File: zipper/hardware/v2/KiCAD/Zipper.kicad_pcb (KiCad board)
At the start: 6 copper layers, 107 x 78 mm, 945 parts, among them J1 FX10B-80S/8-SV, J2 FX10B-80S/8-SV, J3 ASP-122952-01_(HSMC), J4 ASP-134604-01, J5 JUMPER2, J6 MINI-USB-UX60A-MB-5ST, J7 PINHEADER2X25, J8 SMA, SW1 SW, SW2 SW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

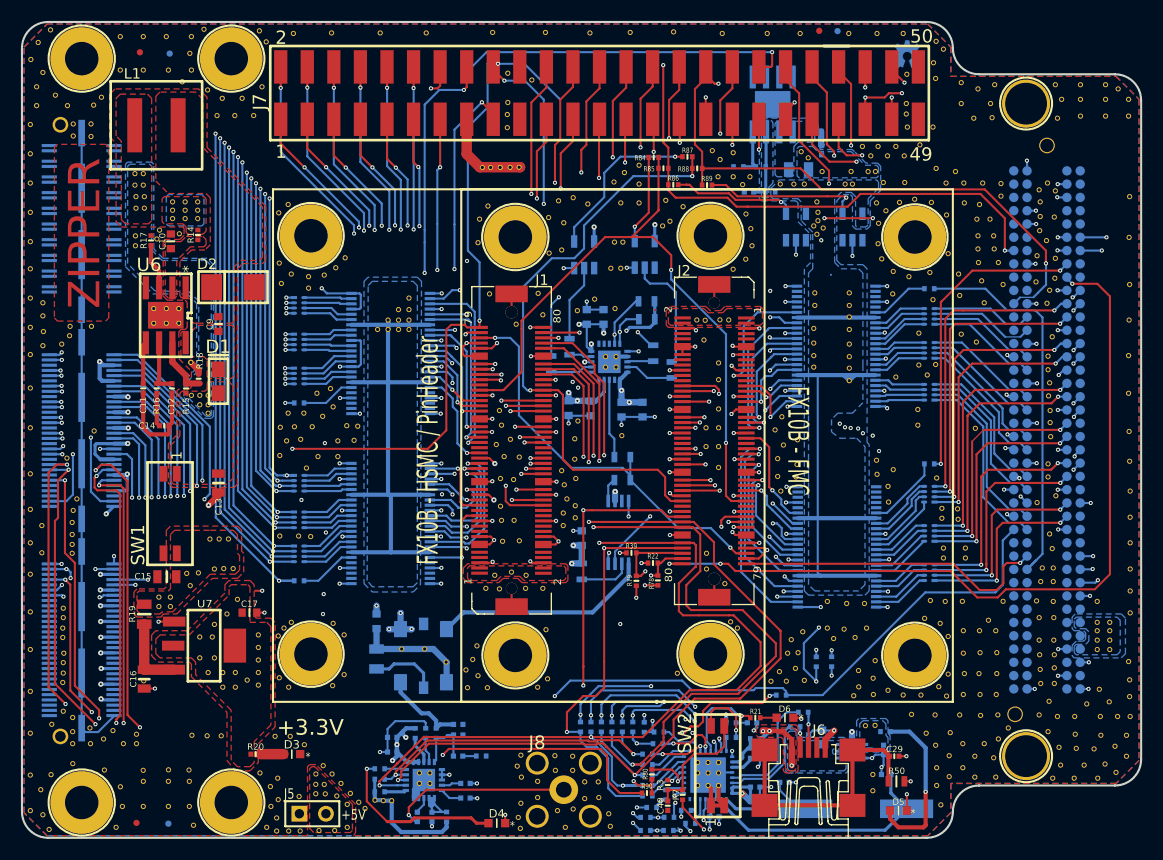
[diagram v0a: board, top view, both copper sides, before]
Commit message: Updated dev kit PDF, and hardware design for placement error
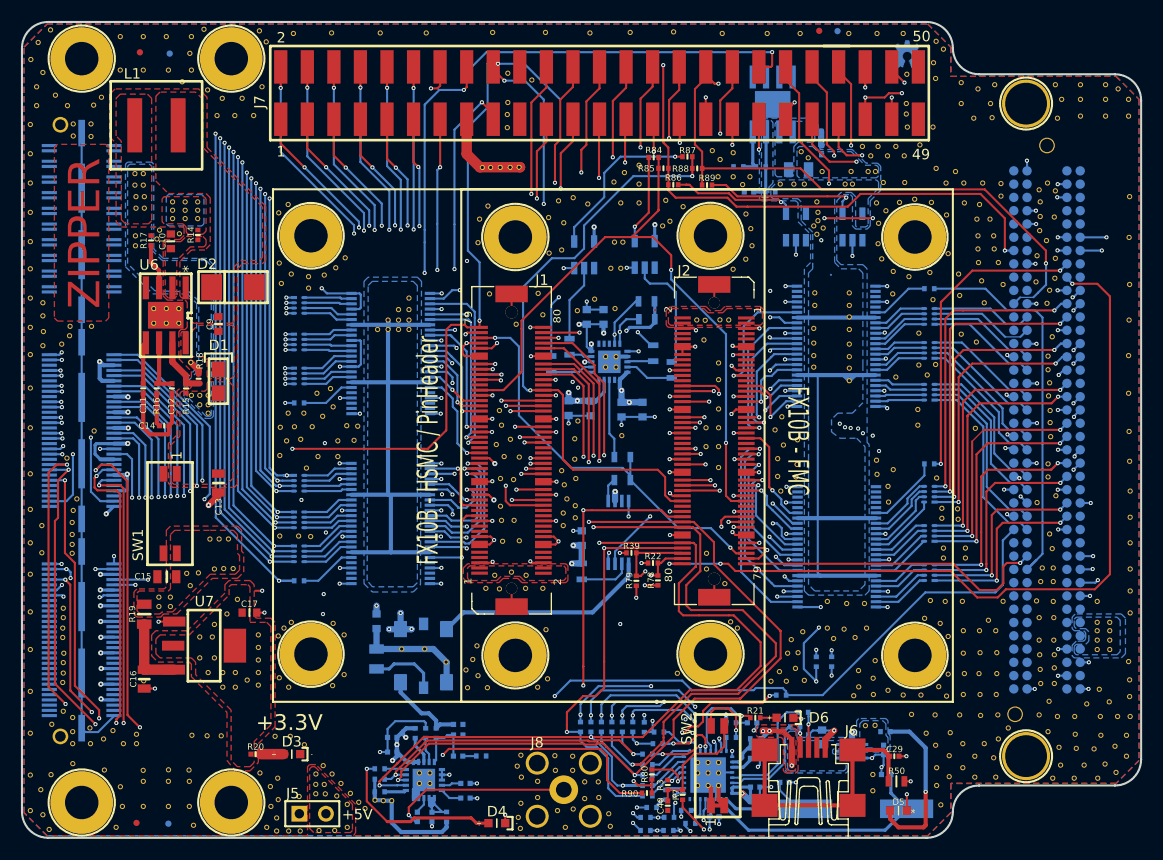
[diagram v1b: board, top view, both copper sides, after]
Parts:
- R84, R86, R87, R89: value 0R_0603 -> 0R_0402
- R85, R88: value 0R_0603_NF -> 0R_0402_NF
- U15: value AT90USB162-16AU -> AT90USB162-16MU
- moved U10 13.7 mm to (167.7, 100.4), turned to 180 degrees
- moved U14 13.7 mm to (117.5, 93.5), turned to 0 degrees
- renumbered U17 to U1, U18 to U12, U1 to X2, U12 to X3
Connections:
- R29 pad 5: N-00000401 -> N-00000399
- R29 pad 6: N-00000407 -> N-00000433
- R29 pad 7: N-00000394 (its old number) -> N-00000402
- R29 pad 8: N-00000397 -> N-00000404
- R30 pad 5: N-00000396 -> N-00000403
- R30 pad 6: N-00000398 -> N-00000405
- R30 pad 7: N-00000410 -> N-00000407
- R30 pad 8: N-00000402 -> N-00000397
- R31 pad 5: N-00000404 -> N-00000431
- R31 pad 6: N-00000406 -> N-00000432
- R31 pad 7: N-00000408 -> N-00000400
- R31 pad 8: N-00000400 -> N-00000401
- R32 pad 1: N-00000432 -> N-00000430
- R46 pad 5: N-00000421 -> N-00000409
- R46 pad 6: N-00000418 -> N-00000395
- R46 pad 7: N-00000424 (its old number) -> N-00000415
- R46 pad 8: N-00000411 (its old number) -> N-00000417
- R47 pad 5: N-00000414 -> N-00000416
- R47 pad 6: N-00000412 (its old number) -> N-00000418
- R47 pad 7: N-00000393 (its old number) -> N-00000419
- R47 pad 8: N-00000439 (its old number) -> N-00000421
- R48 pad 5: N-00000390 (its old number) -> N-00000376
- R48 pad 6: N-00000389 (its old number) -> N-00000377
- R48 pad 7: N-00000374 -> N-00000378
- R48 pad 8: N-00000423 -> N-00000414
- R49 pad 1: N-00000373 -> N-00000375
- U10 pad 11: RXD6_FM -> N-00000400
- U10 pad 12: RXD7_FM -> N-00000401
- U10 pad 13: RXD8_FM -> N-00000403
- U10 pad 14: RXD9_FM -> N-00000405
- U10 pad 16: RXD10_FM -> N-00000407
- U10 pad 17: RXD11_FM -> N-00000397
- U10 pad 19: RXIQSEL_FM -> N-00000399
- U10 pad 2: RXD0_FM -> (no net)
- U10 pad 20: (no net) -> N-00000433
- U10 pad 22: (no net) -> N-00000402
- U10 pad 23: (no net) -> N-00000404
- U10 pad 26: (no net) -> RXD0_FM
- U10 pad 27: (no net) -> RXD1_FM
- U10 pad 29: (no net) -> RXD2_FM
- U10 pad 3: RXD1_FM -> (no net)
- U10 pad 30: N-00000432 -> RXD3_FM
- U10 pad 32: N-00000404 -> RXD4_FM
- U10 pad 33: N-00000406 -> RXD5_FM
- U10 pad 35: N-00000408 -> RXD6_FM
- U10 pad 36: N-00000400 -> RXD7_FM
- U10 pad 37: N-00000396 -> RXD8_FM
- U10 pad 38: N-00000398 -> RXD9_FM
- U10 pad 40: N-00000410 -> RXD10_FM
- U10 pad 41: N-00000402 -> RXD11_FM
- U10 pad 43: N-00000401 -> RXIQSEL_FM
- U10 pad 44: N-00000407 -> (no net)
- U10 pad 46: N-00000394 (its old number) -> (no net)
- U10 pad 47: N-00000397 -> (no net)
- U10 pad 5: RXD2_FM -> (no net)
- U10 pad 6: RXD3_FM -> N-00000430
- U10 pad 8: RXD4_FM -> N-00000431
- U10 pad 9: RXD5_FM -> N-00000432
- U14 pad 11: RXD7_HM -> N-00000378
- U14 pad 12: RXD6_HM -> N-00000414
- U14 pad 13: RXD9_HM -> N-00000416
- U14 pad 14: RXD8_HM -> N-00000418
- U14 pad 16: RXD11_HM -> N-00000419
- U14 pad 17: RXD10_HM -> N-00000421
- U14 pad 19: RXIQSEL_HM -> N-00000409
- U14 pad 2: RXD1_HM -> (no net)
- U14 pad 20: (no net) -> N-00000395
- U14 pad 22: (no net) -> N-00000415
- U14 pad 23: (no net) -> N-00000417
- U14 pad 26: (no net) -> RXD1_HM
- U14 pad 27: (no net) -> RXD0_HM
- U14 pad 29: (no net) -> RXD3_HM
- U14 pad 3: RXD0_HM -> (no net)
- U14 pad 30: N-00000373 -> RXD2_HM
- U14 pad 32: N-00000390 (its old number) -> RXD5_HM
- U14 pad 33: N-00000389 (its old number) -> RXD4_HM
- U14 pad 35: N-00000374 -> RXD7_HM
- U14 pad 36: N-00000423 -> RXD6_HM
- U14 pad 37: N-00000414 -> RXD9_HM
- U14 pad 38: N-00000412 (its old number) -> RXD8_HM
- U14 pad 40: N-00000393 (its old number) -> RXD11_HM
- U14 pad 41: N-00000439 (its old number) -> RXD10_HM
- U14 pad 43: N-00000421 -> RXIQSEL_HM
- U14 pad 44: N-00000418 -> (no net)
- U14 pad 46: N-00000424 (its old number) -> (no net)
- U14 pad 47: N-00000411 (its old number) -> (no net)
- U14 pad 5: RXD3_HM -> (no net)
- U14 pad 6: RXD2_HM -> N-00000375
- U14 pad 8: RXD5_HM -> N-00000376
- U14 pad 9: RXD4_HM -> N-00000377
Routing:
- net N-00000430: track 0.00 -> 7.20 mm
- net N-00000408: track 6.82 -> 0.00 mm
- net N-00000406: track 6.41 -> 0.00 mm
- net N-00000431: track 0.00 -> 6.33 mm
- net N-00000410: track 5.74 -> 0.00 mm
- net N-00000394 (its old number): track 5.71 -> 0.00 mm
- net N-00000403: track 0.00 -> 5.53 mm
- net N-00000396: track 5.53 -> 0.00 mm
- net N-00000405: track 0.00 -> 5.53 mm
- net N-00000398: track 5.53 -> 0.00 mm
- net N-00000399: track 0.00 -> 5.26 mm
- net N-00000433: track 0.00 -> 5.22 mm
- net N-00000375: track 0.00 -> 5.14 mm
- net N-00000373: track 5.14 -> 0.00 mm
- net N-00000378: track 0.00 -> 4.98 mm
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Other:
- board text added: "/"
- board text added: "Board v.2 r.2"
